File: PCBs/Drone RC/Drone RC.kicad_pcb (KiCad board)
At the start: 2 copper layers, 111 x 48 mm, 50 parts, among them J1 BATTERY_1S, J2 RW1, J3 RW2, J7 SWD_HEADER, J8 CHARGE_PORT, SW1 SW_Push, SW2 SW_Push_2, SW3 SW_Push_3, SW4 SW_Push_4, SW5 SW_Push_5, SW6 SW_Push_6, SW7 SW_Push_7, SW8 SW_Push_8, SW9 SLIDE_SWITCH, U1 AMS1117-3.3, U4 STM32F103C8T6, U5 BK2423, Y2 16MHz, Y3 16MHz

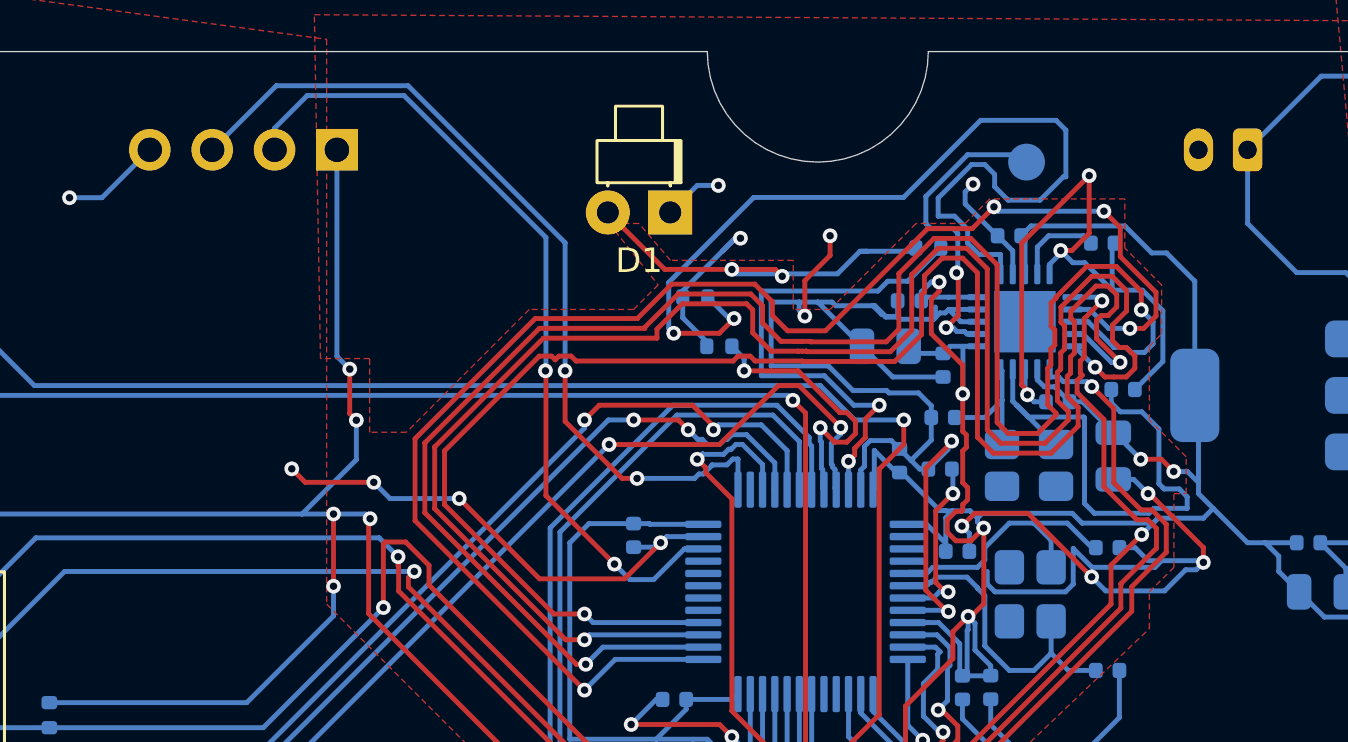
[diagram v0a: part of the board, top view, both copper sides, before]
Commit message: added fixed PCBs
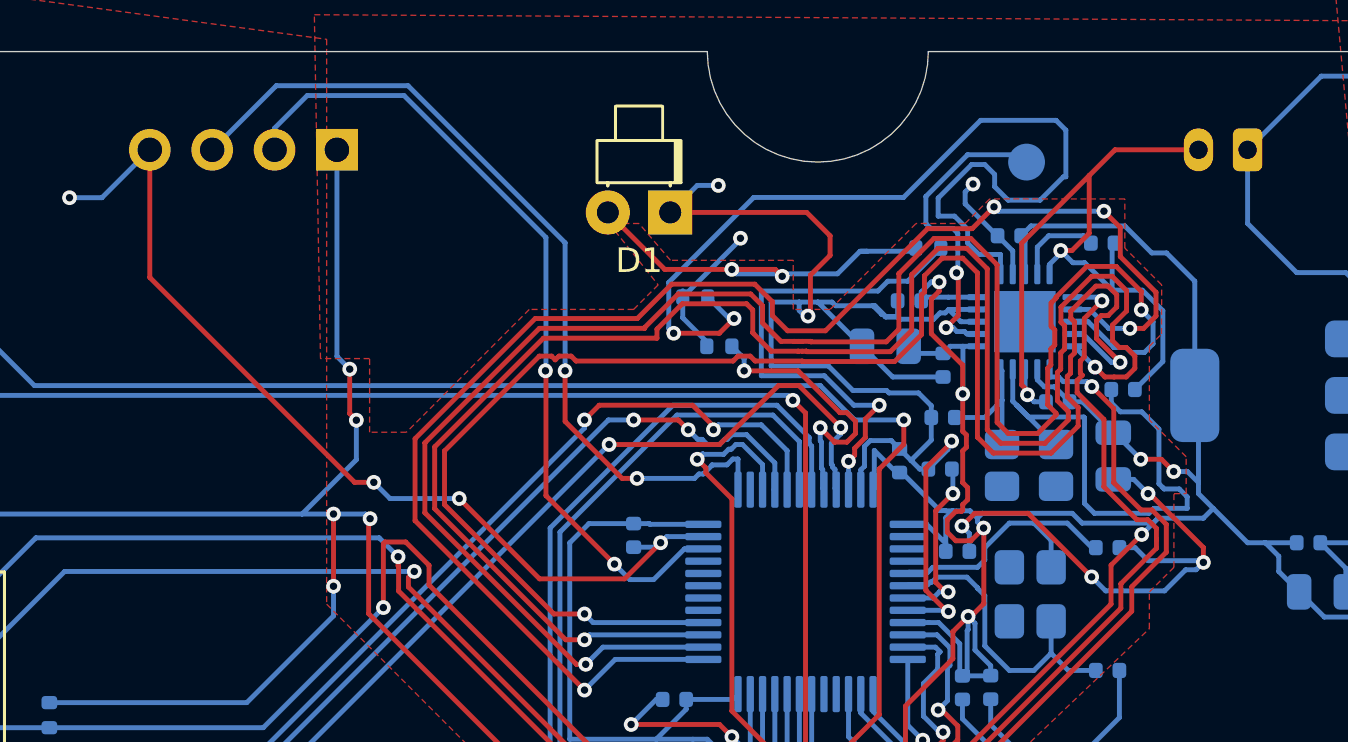
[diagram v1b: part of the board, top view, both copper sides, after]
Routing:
- net GND: track 329.9 -> 345.2 mm, vias 35 -> 32
